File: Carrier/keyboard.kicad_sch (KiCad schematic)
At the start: 27 parts, among them SW11 SW_Push, SW12 SW_Push, SW13 SW_Push, SW14 SW_Push, SW15 SW_Push, SW16 SW_Push, SW17 SW_Push, SW18 SW_Push, SW19 SW_Push, U1 TCA8418, U15 AP3032

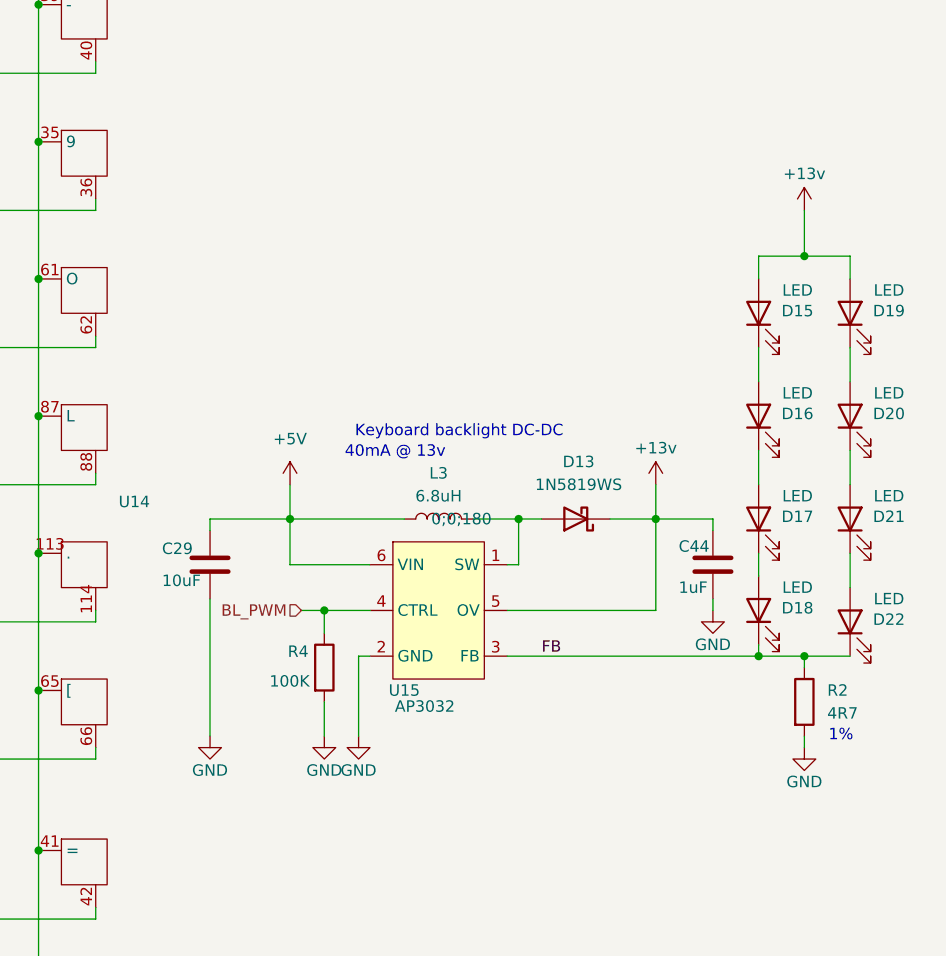
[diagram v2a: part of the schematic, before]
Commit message: Started ripping parts out
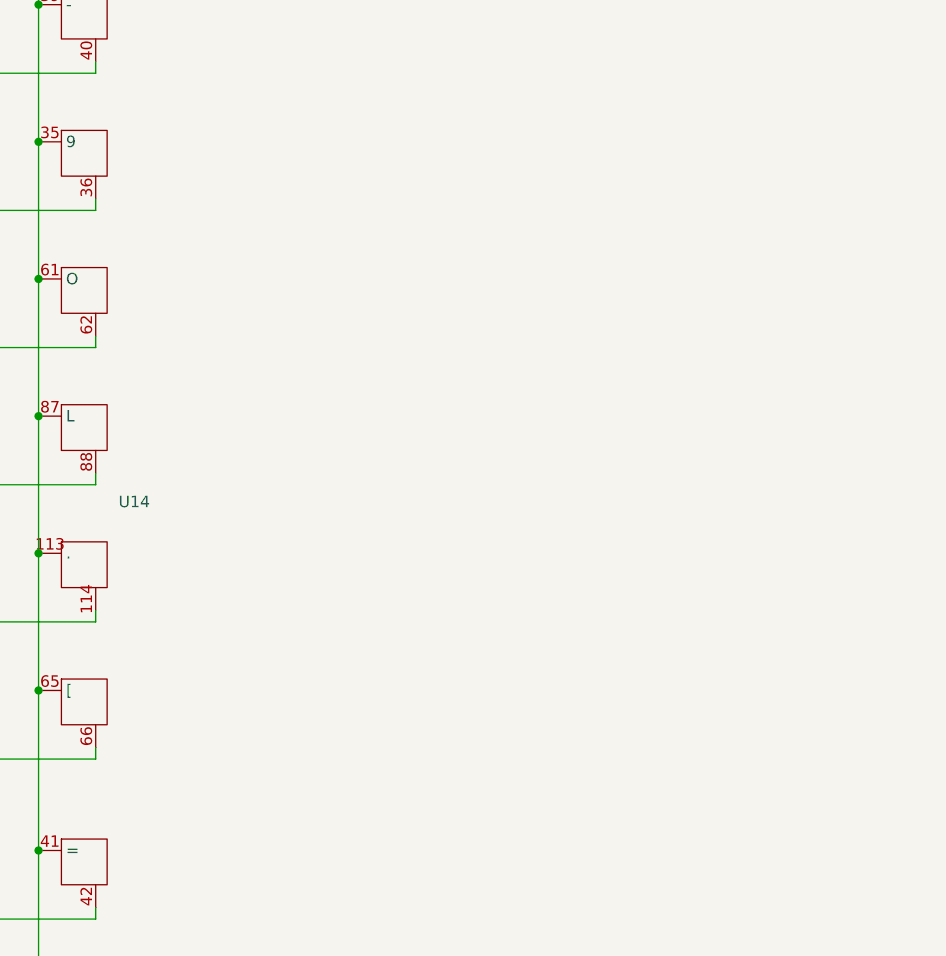
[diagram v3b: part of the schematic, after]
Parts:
- removed C29: 10uF, Capacitor_SMD:C_0603_1608Metric, symbol Device:C
- removed C44: 1uF, Capacitor_SMD:C_0402_1005Metric, symbol Device:C
- removed D13: 1N5819WS, Diode_SMD:D_SOD-323, symbol Device:D_Schottky
- removed D15, D16, D17, D18, D19, D20, D21, D22: LED, keyboard_leds:LTW-010DCG, symbol Device:LED
- removed L3: 6.8uH, Inductor_SMD:L_Vishay_IFSC-1515AH_4x4x1.8mm, symbol Device:L
- removed R2: 4R7, Resistor_SMD:R_0402_1005Metric, symbol Device:R
- removed R4: 100K, Resistor_SMD:R_0402_1005Metric, symbol Device:R
- removed U15: AP3032, Package_TO_SOT_SMD:SOT-23-6_Handsoldering, symbol AP3032:AP3032
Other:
- note removed: "1%"
- note removed: "40mA @ 13v"
- note removed: "Keyboard backlight DC-DC"

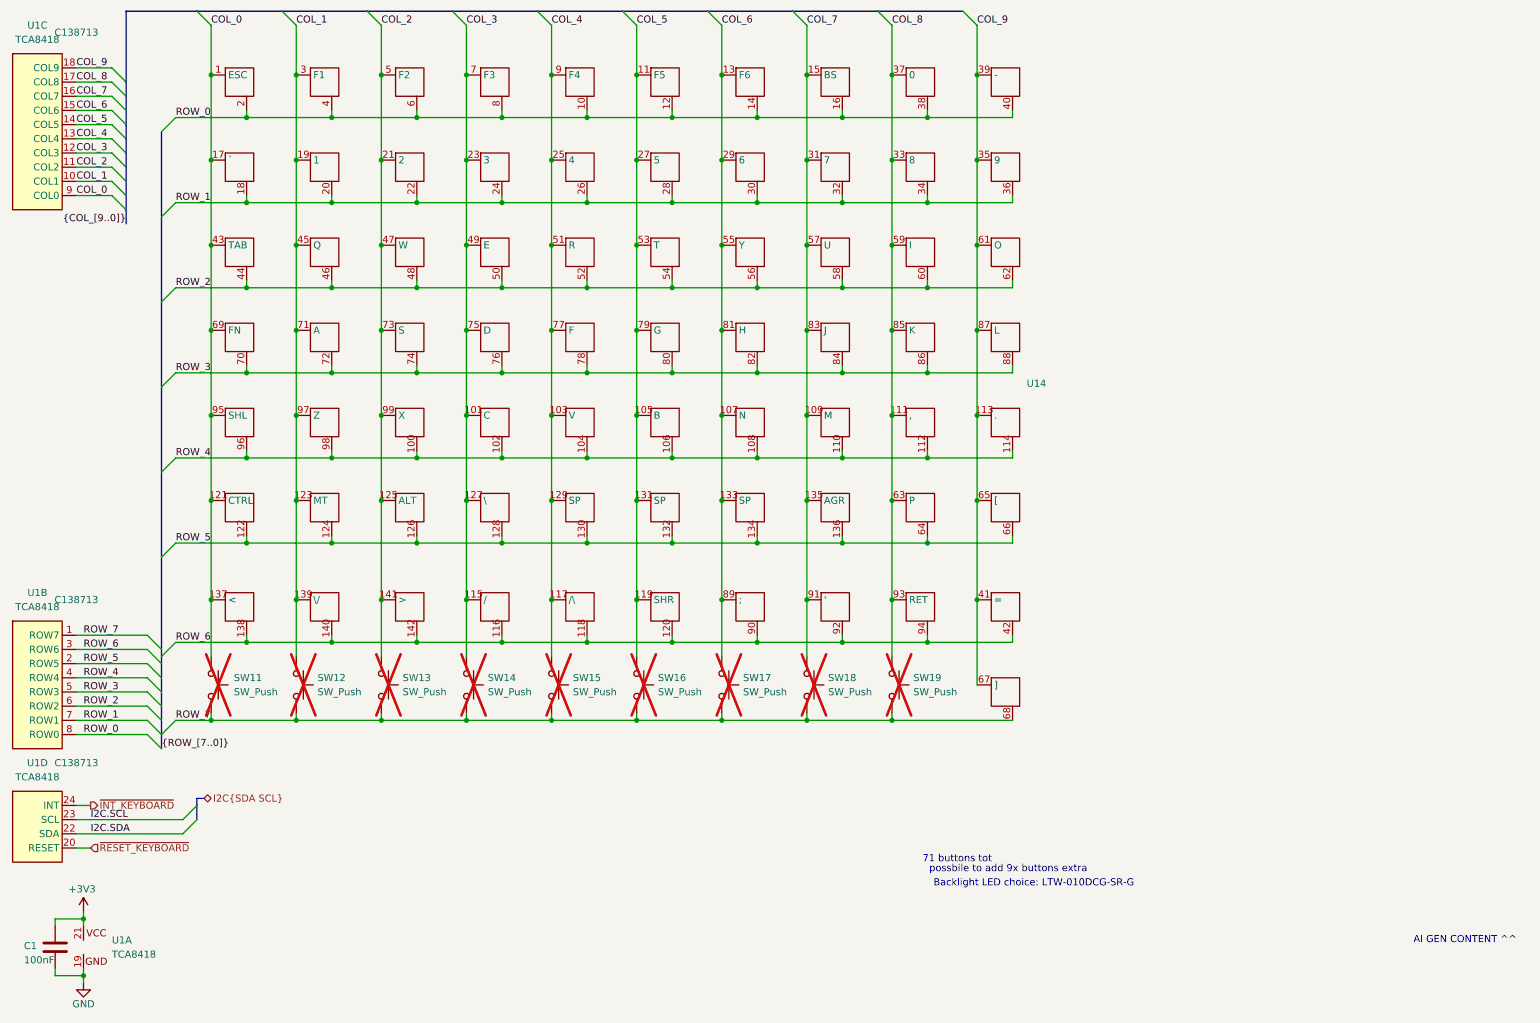
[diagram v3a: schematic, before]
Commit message: Pulled out some stuff I don't need.
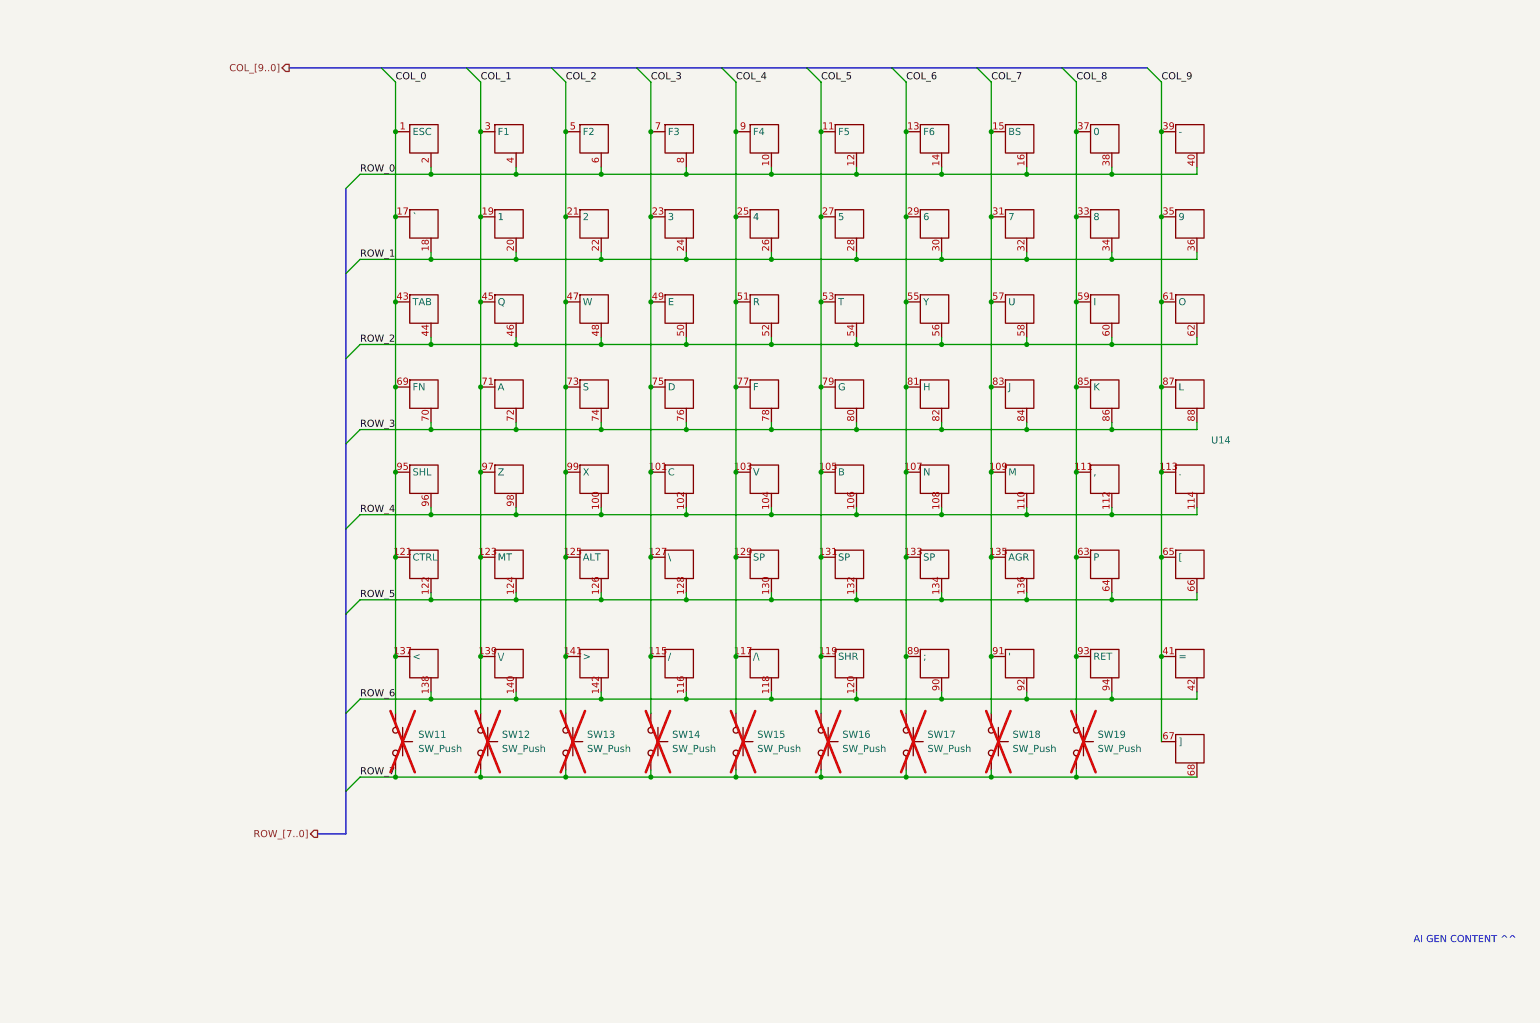
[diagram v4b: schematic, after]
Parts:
- removed C1: 100nF, Capacitor_SMD:C_0402_1005Metric, symbol Device:C
- removed U1: TCA8418, TCA8418RTWR:QFN50P400X400X80-25N, symbol tca8418:TCA8418
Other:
- note removed: "71 buttons tot"
- note removed: "Backlight LED choice: LTW-010DCG-SR-G"
- note removed: "possbile to add 9x buttons extra"
- moved on the sheet: SW11, SW12, SW13, SW14, SW15, SW16, SW17, SW18, SW19, U14
